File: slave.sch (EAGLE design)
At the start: 363 parts, among them J2 EB21A-06-D, J3 EB21A-06-D, J4 EB21A-06-D, J5 EB21A-06-D, J6 282837-9, J7 282837-9, J8 282837-9, J9 1715250000, Q1 DMN2056U-7, Q10 DMN2056U-7, Q11 DMN2056U-7, Q12 DMN2056U-7, Q13 DMN2056U-7, Q14 DMN2056U-7, Q15 DMN2056U-7, Q16 DMN2056U-7, Q17 DMN2056U-7, Q18 DMN2056U-7, Q19 DMN2056U-7, Q2 DMN2056U-7, Q20 DMN2056U-7, Q21 DMN2056U-7, Q22 DMN2056U-7, Q23 DMN2056U-7, Q24 DMN2056U-7, Q25 DMN2056U-7, Q26 DMN2056U-7, Q27 DMN2056U-7, Q28 DMN2056U-7, Q29 DMN2056U-7, Q3 DMN2056U-7, Q30 DMN2056U-7, Q31 DMN2056U-7, Q32 DMN2056U-7, Q33 DMN2056U-7, Q34 DMN2056U-7, Q35 DMN2056U-7, Q36 DMN2056U-7, Q37 DMN2056U-7, Q38 DMN2056U-7, Q39 DMN2056U-7, Q4 DMN2056U-7, Q40 DMN2056U-7, Q41 DMN2056U-7, Q42 DMN2056U-7, Q5 DMN2056U-7, Q7 DMN2056U-7, Q8 DMN2056U-7, Q9 DMN2056U-7, U1 INA332AIDGKR, U10 INA332AIDGKR, U11 INA332AIDGKR, U12 INA332AIDGKR, U13 INA332AIDGKR, U14 INA332AIDGKR, U15 INA332AIDGKR, U16 INA332AIDGKR, U17 INA332AIDGKR, U18 INA332AIDGKR, U19 INA332AIDGKR, U2 AP2112K-3.3TRG1, U20 INA332AIDGKR, U21 INA332AIDGKR, U22 INA332AIDGKR, U23 INA332AIDGKR, U24 INA332AIDGKR, U25 INA332AIDGKR, U26 INA332AIDGKR, U27 INA332AIDGKR, U28 INA332AIDGKR, U3 MCP23008-E/P, U4 MCP23008-E/P, U5 MCP23008-E/P, U6 MC74HCT4851ADR2G, U7 MC74HCT4851ADR2G, U8 MC74HCT4851ADR2G, U9 MC74HCT4851ADR2G

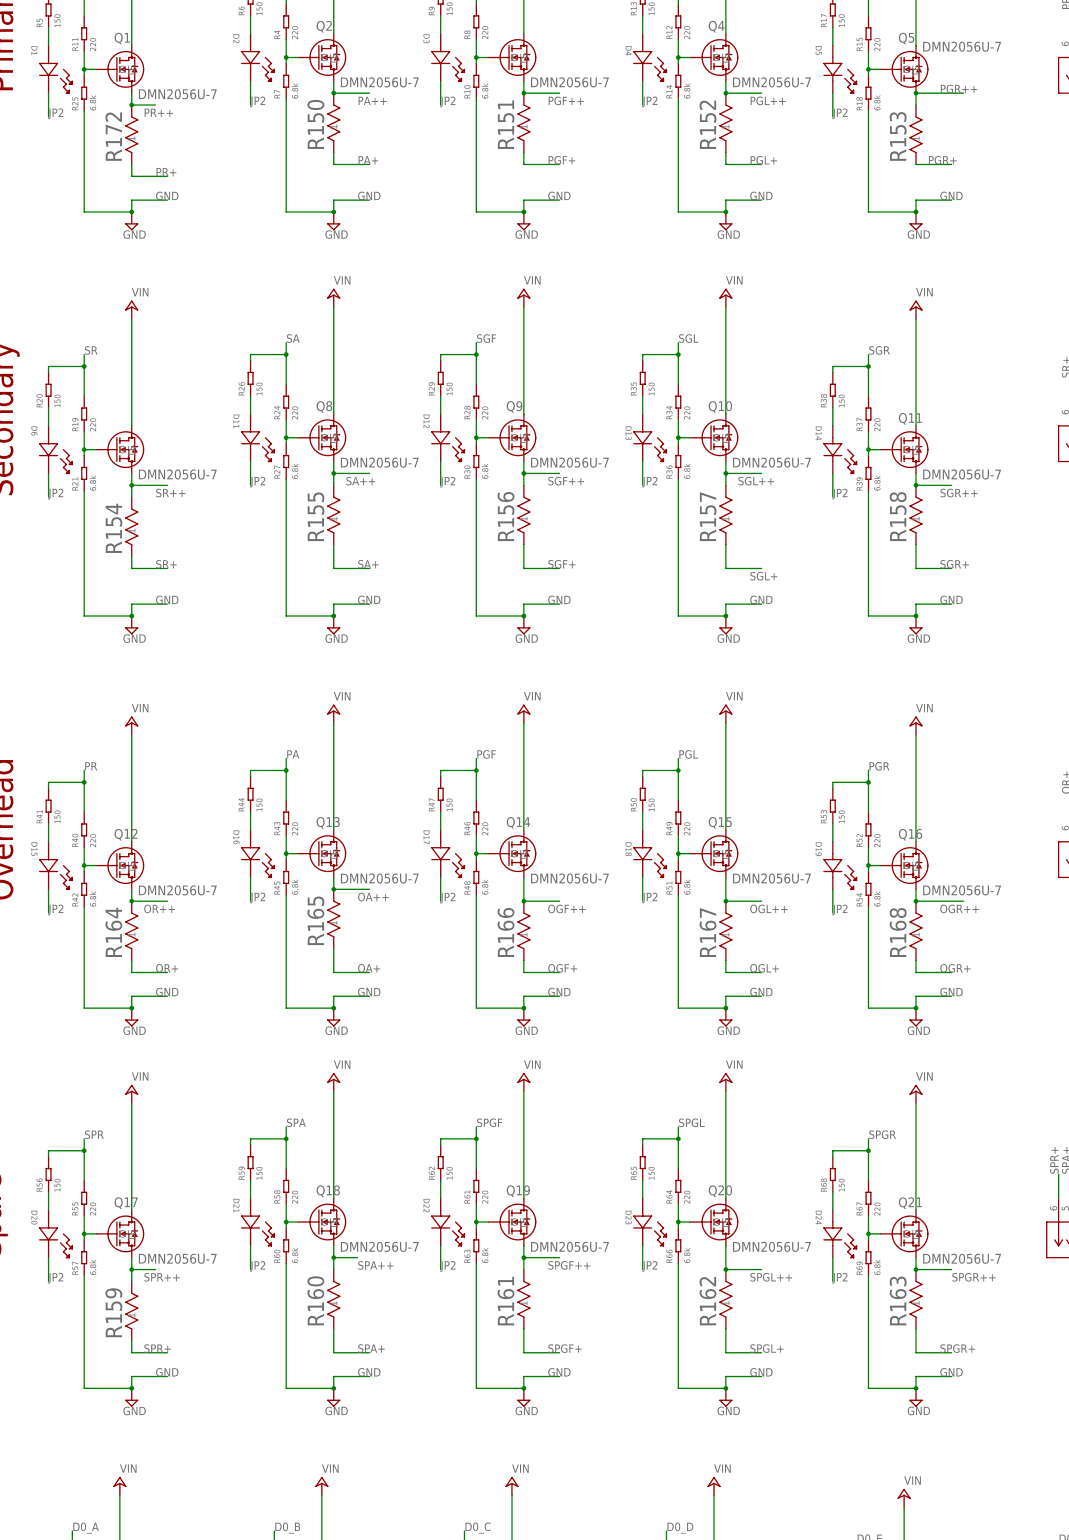
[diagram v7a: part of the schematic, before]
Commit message: added new 100 mOhm shunt resistor for current sensing
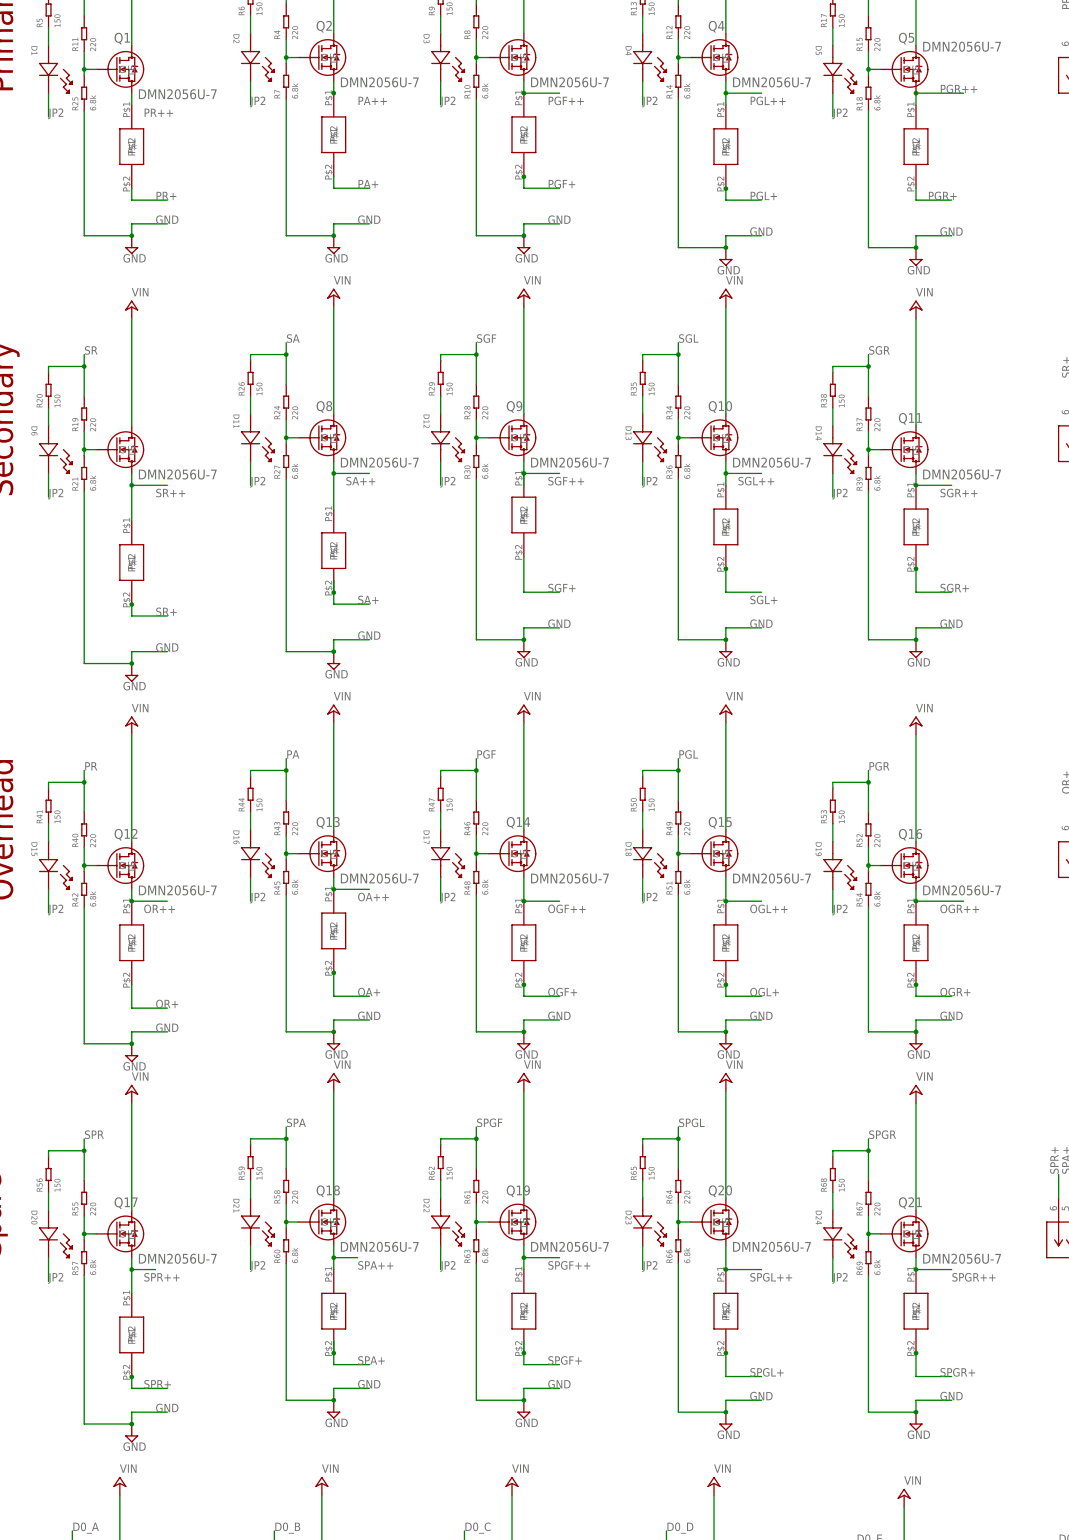
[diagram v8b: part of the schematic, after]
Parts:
- removed R150, R151, R152, R153, R154, R155, R156, R157, R158, R159, R160, R161, R162, R163, R164, R165, R166, R167, R168, R172: 1m, RLC16-R100JTP - 100mOhm:RLC16-R100JTP
- added U$1, U$10, U$11, U$12, U$13, U$14, U$15, U$16, U$17, U$18, U$19, U$2, U$20, U$21, U$4, U$5, U$6, U$7, U$8, U$9: YLR12-2-100F, YLR12-2-100F:YLR12-2-100F
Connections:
- net OA+: now also U$15.P$2; no longer R165.1
- net OA++: now also U$15.P$1; no longer R165.2
- net OGF+: now also U$14.P$2; no longer R166.1
- net OGF++: now also U$14.P$1; no longer R166.2
- net OGL+: now also U$13.P$2; no longer R167.1
- net OGL++: now also U$13.P$1; no longer R167.2
- net OGR+: now also U$12.P$2; no longer R168.1
- net OGR++: now also U$12.P$1; no longer R168.2
- net OR+: now also U$16.P$2; no longer R164.1
- net OR++: now also U$16.P$1; no longer R164.2
- net PA+: now also U$2.P$2; no longer R150.1
- net PA++: now also U$2.P$1; no longer R150.2
- net PGF+: now also U$4.P$2; no longer R151.1
- net PGF++: now also U$4.P$1; no longer R151.2
- net PGL+: now also U$5.P$2; no longer R152.1
- net PGL++: now also U$5.P$1; no longer R152.2
- net PGR+: now also U$6.P$2; no longer R153.1
- net PGR++: now also U$6.P$1; no longer R153.2
- net PR+: now also U$1.P$2; no longer R172.1
- net PR++: now also U$1.P$1; no longer R172.2
- net SA+: now also U$8.P$2; no longer R155.1
- net SA++: now also U$8.P$1; no longer R155.2
- net SGF+: now also U$9.P$2; no longer R156.1
- net SGF++: now also U$9.P$1; no longer R156.2
- net SGL+: now also U$10.P$2; no longer R157.1
- net SGL++: now also U$10.P$1; no longer R157.2
- net SGR+: now also U$11.P$2; no longer R158.1
- net SGR++: now also U$11.P$1; no longer R158.2
- net SPA+: now also U$18.P$2; no longer R160.1
- net SPA++: now also U$18.P$1; no longer R160.2
- net SPGF+: now also U$19.P$2; no longer R161.1
- net SPGF++: now also U$19.P$1; no longer R161.2
- net SPGL+: now also U$20.P$2; no longer R162.1
- net SPGL++: now also U$20.P$1; no longer R162.2
- net SPGR+: now also U$21.P$2; no longer R163.1
- net SPGR++: now also U$21.P$1; no longer R163.2
- net SPR+: now also U$17.P$2; no longer R159.1
- net SPR++: now also U$17.P$1; no longer R159.2
- net SR+: now also U$7.P$2; no longer R154.1
- net SR++: now also U$7.P$1; no longer R154.2
